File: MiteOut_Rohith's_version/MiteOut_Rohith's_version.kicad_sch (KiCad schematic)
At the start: 28 parts, among them J1 JST, U1 ESP32-S3-WROOM-1, U2 INA260, U3 BQ25185DLHR, U4 TPS61022

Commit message: finished batt board
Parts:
- removed J1: JST, Connector_JST:JST_XH_S2B-XH-A_1x02_P2.50mm_Horizontal, symbol Connector_Generic:Conn_01x02
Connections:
- net IN- is gone; now on net GND: U2.14 (IN-), U2.15 (IN-), U2.16 (IN-)
- net IN+: now also C5.1, U3.2 (BAT)
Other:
- moved on the sheet: C2, C3, C4, D1, D2, D3, D4, D5, R10, R11, R5, R6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

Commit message: quick fix
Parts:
- removed C2: C, symbol Device:C
- removed R5: R, symbol Device:R
- added C6, C7: 22uF, symbol Device:C
- added J1: JST, Connector_JST:JST_XH_S2B-XH-A_1x02_P2.50mm_Horizontal, symbol Connector_Generic:Conn_01x02
- added R13: 732k, symbol Device:R
- added R14: 100k, symbol Device:R
- added R15: 22k, symbol Device:R
- added SW1: SW_SPST, symbol Switch:SW_SPST
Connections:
- net GND: now also C5.1, D3.2 (A), C6.1, C6.2, C7.1, C7.2, J1.2 (Pin_2), R13.1, R14.1, R15.2, SW1.1 (A); no longer C5.2
- net IN+: now also C5.2, J1.1 (Pin_1); no longer C5.1
- net VBUS: now reaches D5.2 (A)
- net V+: now reaches R12.2
- net V+: now also L1.1, U3.1 (SYS), U4.7 (VIN)
- net at D3.1 (K): now also R15.1
- net VIN/Solar+: now reaches D4.2 (A)
- net at U4.3 (VOUT): now also R13.2
- net at U4.4 (FB): now also R14.2
- new net +5V: SW1.2 (B)
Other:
- moved on the sheet: C3, C4, D1, D2, D3, D4, D5, L1, R10, R11, R12, R6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

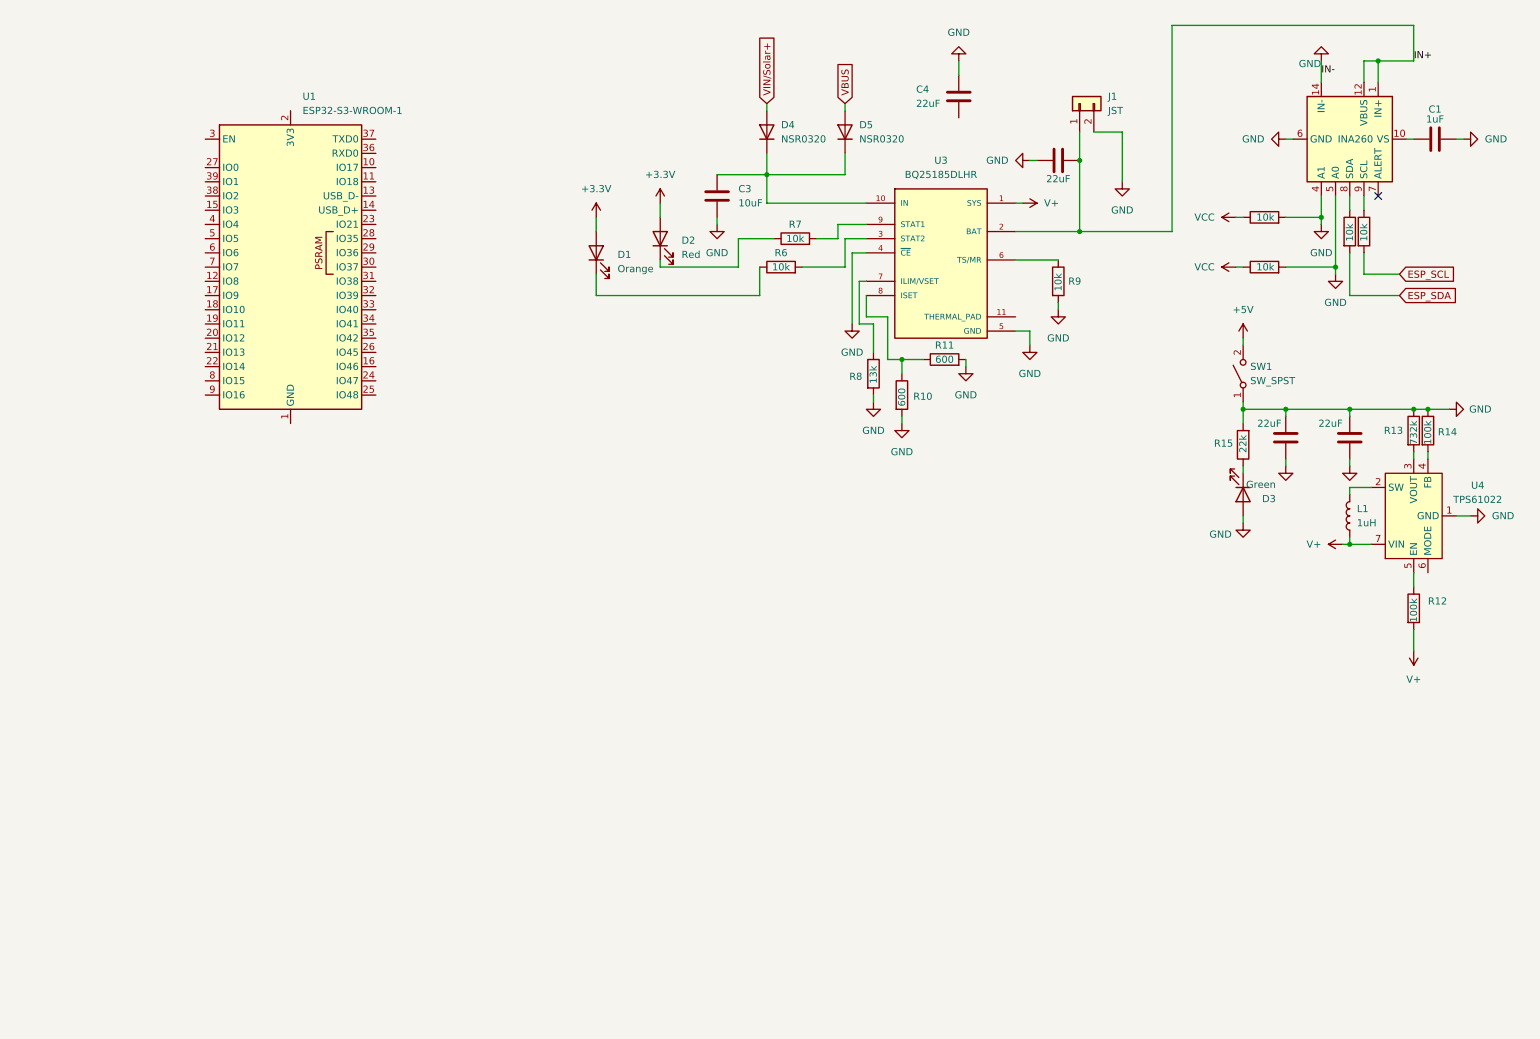
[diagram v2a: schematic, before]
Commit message: added SD Card
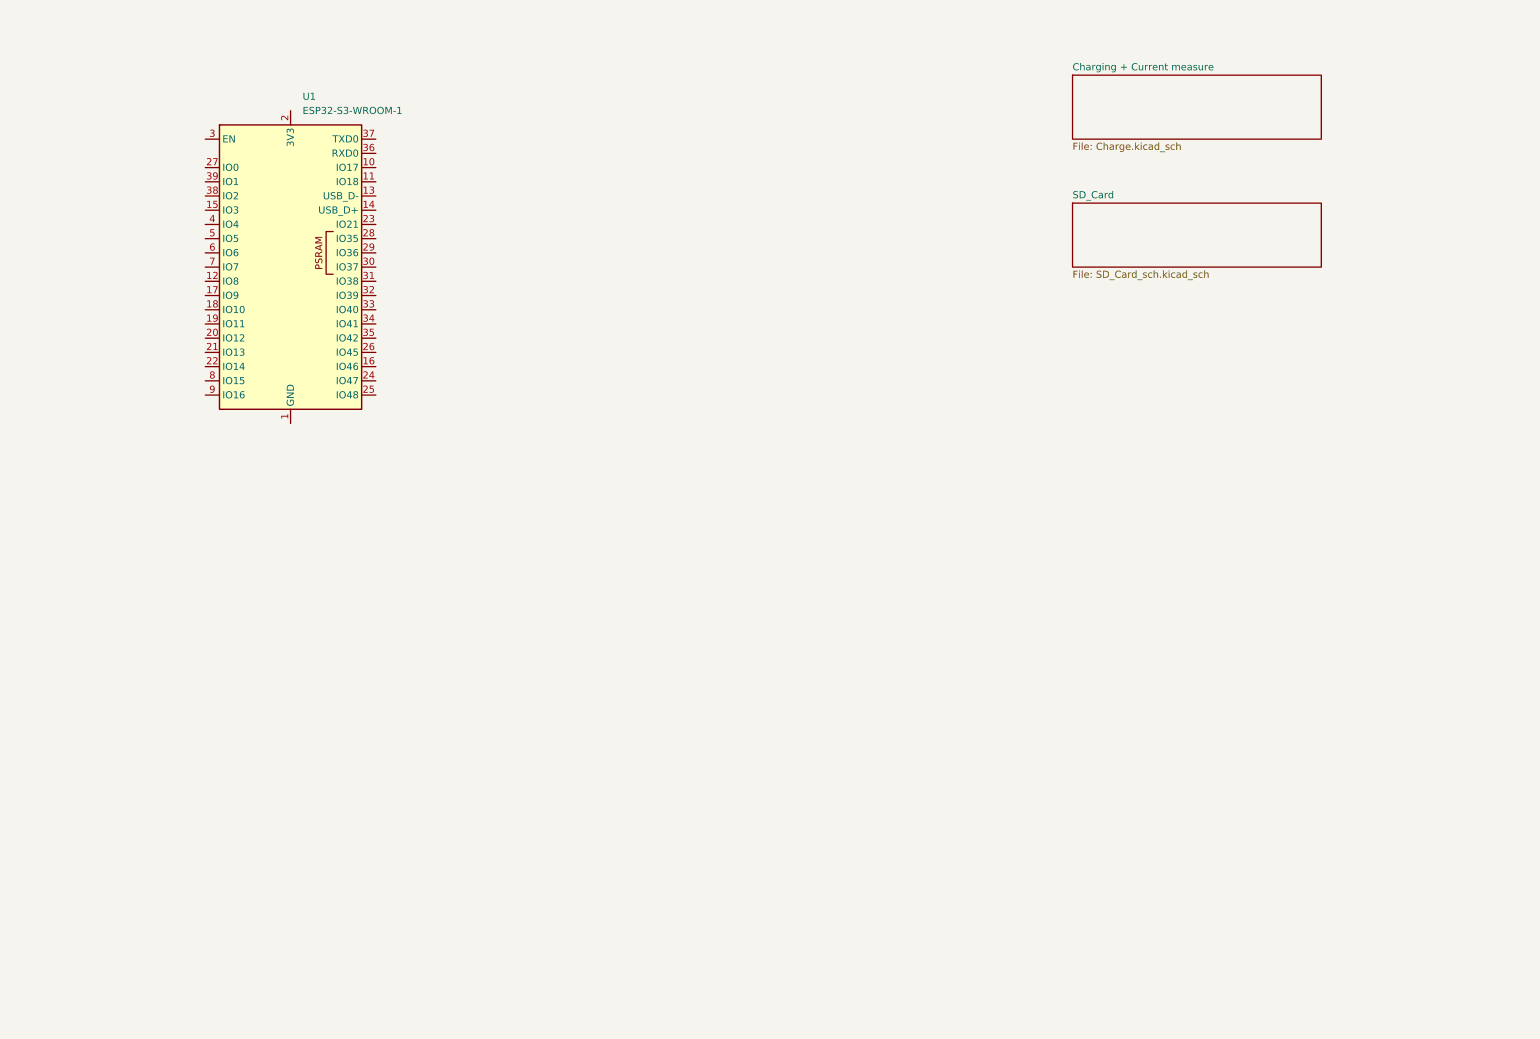
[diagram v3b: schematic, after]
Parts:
- removed C1: 1uF, symbol Device:C
- removed C3: 10uF, symbol Device:C
- removed C4, C5, C6, C7: 22uF, symbol Device:C
- removed D1: Orange, symbol Device:LED
- removed D2: Red, symbol Device:LED
- removed D3: Green, symbol Device:LED
- removed D4, D5: NSR0320, symbol Device:D
- removed J1: JST, Connector_JST:JST_XH_S2B-XH-A_1x02_P2.50mm_Horizontal, symbol Connector_Generic:Conn_01x02
- removed L1: 1uH, symbol Device:L
- removed R1, R2, R3, R4, R6, R7, R9: 10k, symbol Device:R
- removed R10, R11: 600, symbol Device:R
- removed R12, R14: 100k, symbol Device:R
- removed R13: 732k, symbol Device:R
- removed R15: 22k, symbol Device:R
- removed R8: 13k, symbol Device:R
- removed SW1: SW_SPST, symbol Switch:SW_SPST
- removed U2: INA260, Package_SO:TSSOP-16_4.4x5mm_P0.65mm, symbol Sensor_Energy:INA260
- removed U3: BQ25185DLHR, BQ25185DLHR:IC_BQ25185DLHR, symbol BQ25185DLHR:BQ25185DLHR
- removed U4: TPS61022, Package_DFN_QFN:Texas_RWU0007A_VQFN-7_2x2mm_P0.5mm, symbol Converter_DCDC:TPS61022
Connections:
- no-connect marks 1 -> 0
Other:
- added sheet Charging + Current measure (Charge.kicad_sch)
- added sheet SD_Card (SD_Card_sch.kicad_sch)

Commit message: Finished ADC + ESP needing edits
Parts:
- added C18, C19, C21: .1uF, Capacitor_SMD:C_0603_1608Metric_Pad1.08x0.95mm_HandSolder, symbol Device:C
- added C20: 22uf, Capacitor_SMD:C_0603_1608Metric_Pad1.08x0.95mm_HandSolder, symbol Device:C
- added C22, C23: 10uF, symbol Device:C
- added D11: LED, LED_SMD:LED_0603_1608Metric_Pad1.05x0.95mm_HandSolder, symbol Device:LED
- added D4: WS2812B, LED_SMD:LED_WS2812B_PLCC4_5.0x5.0mm_P3.2mm, symbol LED:WS2812B
- added J4: USB_C_Receptacle_USB2.0_16P, Connector_USB:USB_C_Receptacle_GCT_USB4105-xx-A_16P_TopMnt_Horizontal, symbol Connector:USB_C_Receptacle_USB2.0_16P
- added R29, R30, R31: 10k, Resistor_SMD:R_0603_1608Metric_Pad0.98x0.95mm_HandSolder, symbol Device:R
- added R32, R33, R36: 5.1k, symbol Device:R
- added R34: 1M, Resistor_SMD:R_0603_1608Metric_Pad0.98x0.95mm_HandSolder, symbol Device:R
- added R35: 200k, Resistor_SMD:R_0603_1608Metric_Pad0.98x0.95mm_HandSolder, symbol Device:R
- added SW3: RESET, Button_Switch_SMD:SW_SPST_PTS810, symbol Switch:SW_MEC_5E
- added SW4: BOOT, Button_Switch_SMD:SW_SPST_PTS810, symbol Switch:SW_MEC_5E
- added U12: ESP32-S3-MINI-1, RF_Module:ESP32-S2-MINI-1, symbol RF_Module:ESP32-S3-MINI-1
- added U13: D3V3XA4B10LP, Package_DFN_QFN:Diodes_UDFN-10_1x2.5mm_P0.5mm, symbol Power_Protection:D3V3XA4B10LP
- added U14: TLV75801PDRV, Package_SON:WSON-6-1EP_2x2mm_P0.65mm_EP1x1.6mm, symbol Regulator_Linear:TLV75801PDRV
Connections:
- new net: R34.2, R35.1, U14.2 (FB)
- new net: J4.A5 (CC1), R32.1
- new net: J4.B5 (CC2), R33.1
- new net: D4.4 (DIN), U12.30 (IO48)
- new net: D11.1 (K), R36.2
- new net 3V3: C20.1, C21.1, C23.1, D11.2 (A), D4.1 (VDD), R29.1, R30.1, R31.1, R34.1, U12.3 (3V3), U14.1 (OUT)
- new net 5VUSB: C22.1, J4.A4 (VBUS), J4.A9 (VBUS), J4.B4 (VBUS), J4.B9 (VBUS), U13.4, U14.4 (EN), U14.6 (IN)
- new net ESP32_EN: C18.2, R29.2, SW3.3 (K), SW3.4 (A), U12.45 (EN)
- new net GND: C18.1, C19.2, C20.2, C21.2, C22.2, C23.2, D4.3 (VSS), J4.A1 (GND), J4.A12 (GND), J4.B1 (GND), J4.B12 (GND), J4.SH (SHIELD), R32.2, R33.2, R35.2, R36.1, SW3.1, SW3.2, SW4.1, SW4.2, U12.1 (GND), U12.2 (GND), U12.42 (GND), U12.43 (GND), U12.46 (GND), U12.47 (GND), U12.48 (GND), U12.49 (GND), U12.50 (GND), U12.51 (GND), U12.52 (GND), U12.53 (GND), U12.54 (GND), U12.55 (GND), U12.56 (GND), U12.57 (GND), U12.58 (GND), U12.59 (GND), U12.60 (GND), U12.61 (GND), U12.62 (GND), U12.63 (GND), U12.64 (GND), U12.65 (GND), U13.3 (VSS), U13.8 (VSS), U14.3 (GND), U14.7 (GND)
- new net GPIO0: C19.1, SW4.3 (K), SW4.4 (A), U12.4 (IO0)
- new net I2C_SCL: R31.2, U12.21 (IO17)
- new net I2C_SDA: R30.2, U12.22 (IO18)
- new net USB_N: J4.A7 (D-), J4.B7 (D-), U12.23 (USB_D-), U13.2
- new net USB_P: J4.A6 (D+), J4.B6 (D+), U12.24 (USB_D+), U13.1
- no-connect marks 0 -> 2
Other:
- added sheet ADC (ADC.kicad_sch)
- moved on the sheet: U1

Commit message: finished RTC
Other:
- added sheet BME+RTC (BME_RTC.kicad_sch)
- moved on the sheet: C22, C23, D11, J4, R32, R33, R34, R35, R36, U1, U13, U14

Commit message: some changes ig
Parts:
- removed C21: .1uF, Capacitor_SMD:C_0603_1608Metric_Pad1.08x0.95mm_HandSolder, symbol Device:C
- removed D4: WS2812B, LED_SMD:LED_WS2812B_PLCC4_5.0x5.0mm_P3.2mm, symbol LED:WS2812B
- removed R29, R30, R31: 10k, Resistor_SMD:R_0603_1608Metric_Pad0.98x0.95mm_HandSolder, symbol Device:R
- removed SW3: RESET, Button_Switch_SMD:SW_SPST_PTS810, symbol Switch:SW_MEC_5E
- removed SW4: BOOT, Button_Switch_SMD:SW_SPST_PTS810, symbol Switch:SW_MEC_5E
- removed U12: ESP32-S3-MINI-1, RF_Module:ESP32-S2-MINI-1, symbol RF_Module:ESP32-S3-MINI-1
- added C: .1uF, symbol Device:C
- added C16: 22uF, symbol Device:C
- added C17: 10uF, symbol Device:C
- added R14: 10k, symbol Device:R
- added R15: 100, symbol Device:R
- added SW3, SW4: SW_Push, symbol Switch:SW_Push
- added U16: AMS1117CS-3.3, Package_SO:SOIC-8_3.9x4.9mm_P1.27mm, symbol Regulator_Linear:AMS1117CS-3.3
- C18: value .1uF -> 22uF; footprint Capacitor_SMD:C_0603_1608Metric_Pad1.08x0.95mm_HandSolder -> (none)
- C19: footprint Capacitor_SMD:C_0603_1608Metric_Pad1.08x0.95mm_HandSolder -> (none)
- C20: value 22uf -> 1uF; footprint Capacitor_SMD:C_0603_1608Metric_Pad1.08x0.95mm_HandSolder -> (none)
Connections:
- net ESP32_EN is gone; now on net GND: C18.2
- net GPIO0 is gone; now on net +3.3V: C19.1
- net 3V3: no longer C20.1
- net GND: now also U1.1 (GND), U1.40 (GND), U1.41 (GND), C.1, C16.2, C17.1, SW3.1, SW4.1, U16.1 (GND); no longer C18.1
- net +3.3V: now reaches U1.2 (3V3)
- net +3.3V: now also C18.1, C20.1, C.2, C16.1, R14.2, SW3.2, U16.2 (VO), U16.3 (VO), U16.6 (VO), U16.7 (VO)
- net at U1.3 (EN): now also R14.1
- new net: R15.2, SW4.2
- new net +5V: C17.2, U16.4 (VI)
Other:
- moved on the sheet: J4, R32, R33, U1, U13

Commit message: Full Schematic Draft 1
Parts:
- added J9: Conn_01x20_Pin, symbol Connector:Conn_01x20_Pin
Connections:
- net Load_SCL: now reaches U1.10 (IO17)
- net Load_SDA: now reaches U1.11 (IO18)
- net SD_DataOut: now reaches U1.12 (IO8)
- net Data-: now reaches U1.13 (USB_D-)
- net Data+: now reaches U1.14 (USB_D+)
- net GPIO3: now reaches U1.15 (IO3)
- net GPIO3: now also J9.6 (Pin_6)
- net at U1.16 (IO46): now also J9.11 (Pin_11)
- net SD_DataIn: now reaches U1.17 (IO9)
- net SD_CLK: now reaches U1.18 (IO10)
- net CS: now reaches U1.19 (IO11)
- net at U1.20 (IO12): now also J9.1 (Pin_1)
- net at U1.21 (IO13): now also J9.2 (Pin_2)
- net at U1.22 (IO14): now also J9.3 (Pin_3)
- net at U1.23 (IO21): now also J9.18 (Pin_18)
- net at U1.24 (IO47): now also J9.10 (Pin_10)
- net at U1.25 (IO48): now also J9.9 (Pin_9)
- net at U1.26 (IO45): now also J9.12 (Pin_12)
- net at U1.27 (IO0): now also R15.1
- net at U1.31 (IO38): now also J9.17 (Pin_17)
- net at U1.32 (IO39): now also J9.16 (Pin_16)
- net at U1.33 (IO40): now also J9.15 (Pin_15)
- net at U1.34 (IO41): now also J9.14 (Pin_14)
- net at U1.35 (IO42): now also J9.13 (Pin_13)
- net at U1.36 (RXD0): now also J9.19 (Pin_19)
- net at U1.37 (TXD0): now also J9.20 (Pin_20)
- net GPIO2: now reaches U1.38 (IO2)
- net GPIO2: now also J9.7 (Pin_7)
- net GPIO1: now reaches U1.39 (IO1)
- net GPIO1: now also J9.8 (Pin_8)
- net BME(1&2)SDA: now reaches U1.4 (IO4)
- net BME(1&2)SCL: now reaches U1.5 (IO5)
- net BME(3&4)SDA: now reaches U1.6 (IO6)
- net BME(3&4)SCL: now reaches U1.7 (IO7)
- net at U1.8 (IO15): now also J9.4 (Pin_4)
- net at U1.9 (IO16): now also J9.5 (Pin_5)
- no-connect marks 2 -> 5
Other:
- sheet ADC ports: added DataOut, Rate, SCK; removed none
- sheet BME+RTC ports: added BME1SCL, BME1SDA, BME2SCL, BME2SDA, BME3SCL, BME3SDA, BME4SCL, BME4SDA, RTC_SCLK, RTC_SDA, SQW; removed none
- sheet Charging + Current measure ports: added SCK, SDA, VBUS, VIN/Solar+; removed none
- sheet SD_Card ports: added CLK, CS, DataIn, DataOut; removed none
- moved on the sheet: C, C18, C19, C20, C22, C23, D11, R14, R15, R34, R35, R36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

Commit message: some error fixes
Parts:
- renumbered C to C25
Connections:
- net USB_N is gone; now on net Data-: J4.A7 (D-), J4.B7 (D-), U13.2
- net USB_P is gone; now on net Data+: J4.A6 (D+), J4.B6 (D+), U13.1
- net 5VUSB: now also U13.7 (NC)
- net Data+: now also U13.10 (NC)
- net Data-: now also U13.9 (NC)
- no-connect marks 5 -> 7
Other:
- note added: "Notes: - Voltages and Nets for all sheets - SD Card 5V??? - Choose ESP LDO - BME doubled up GPIO - Multi sensor on RTC and single SDA pin"
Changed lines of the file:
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@@
 	(generator_version "10.0")
 	(paper "A4")
+	(text "Notes: \n- Voltages and Nets for all sheets\n- SD Card 5V???\n- Choose ESP LDO\n- BME doubled up GPIO\n- Multi sensor on RTC and single SDA pin"
+		(exclude_from_sim no)
+		(at 164.846 28.702 0)
+		(effects
+			(font
+				(size 2.54 2.54)
+			)
+		)
+	)
 	(junction
 		(at 223.52 74.93)
@@
 	)
 	(junction
-		(at 232.41 99.06)
+		(at 52.07 167.64)
+		(diameter 0)
+		(color 0 0 0 0)
+	)
+	(junction
+		(at 49.53 146.05)
 		(diameter 0)
 		(color 0 0 0 0)
@@
 	)
 	(junction
+		(at 52.07 151.13)
+		(diameter 0)
+		(color 0 0 0 0)
+	)
+	(junction
 		(at 232.41 96.52)
 		(diameter 0)
@@
 	)
 	(junction
+		(at 82.55 172.72)
+		(diameter 0)
+		(color 0 0 0 0)
+	)
+	(junction
 		(at 49.53 24.13)
 		(diameter 0)
@@
 	)
 	(junction
+		(at 54.61 177.8)
+		(diameter 0)
+		(color 0 0 0 0)
+	)
+	(junction
 		(at 54.61 49.53)
 		(diameter 0)
@@
 	)
 	(no_connect
+		(at 82.55 182.88)
+	)
+	(no_connect
 		(at 107.95 67.31)
 	)
@@
 		(at 46.99 160.02)
 	)
+	(no_connect
+		(at 82.55 177.8)
+	)
 	(wire
 		(pts
-			(xy 52.07 172.72) (xy 52.07 151.13)
+			(xy 52.07 172.72) (xy 52.07 167.64)
 		)
 		(stroke
@@
 	(wire
 		(pts
+			(xy 52.07 167.64) (xy 57.15 167.64)
+		)
+		(stroke
+			(width 0)
+			(type default)
+		)
+	)
+	(wire
+		(pts
 			(xy 50.8 63.5) (xy 54.61 63.5)
 		)
@@
 	(wire
 		(pts
+			(xy 52.07 167.64) (xy 52.07 151.13)
+		)
+		(stroke
+			(width 0)
+			(type default)
+		)
+	)
+	(wire
+		(pts
 			(xy 82.55 172.72) (xy 85.09 172.72)
 		)
@@
 	(wire
 		(pts
+			(xy 54.61 182.88) (xy 54.61 177.8)
+		)
+		(stroke
+			(width 0)
+			(type default)
+		)
+	)
+	(wire
+		(pts
 			(xy 130.81 49.53) (xy 130.81 67.31)
 		)
@@
 	(wire
 		(pts
-			(xy 57.15 177.8) (xy 49.53 177.8)
-		)
-		(stroke
-			(width 0)
-			(type default)
-		)
-	)
-	(wire
-		(pts
-			(xy 228.6 99.06) (xy 232.41 99.06)
+			(xy 57.15 177.8) (xy 54.61 177.8)
 		)
 		(stroke
@@
 	(wire
 		(pts
-			(xy 232.41 96.52) (xy 232.41 99.06)
+			(xy 57.15 182.88) (xy 54.61 182.88)
+		)
+		(stroke
+			(width 0)
+			(type default)
+		)
+	)
+	(wire
+		(pts
+			(xy 52.07 151.13) (xy 59.69 151.13)
 		)
 		(stroke
@@
 	(wire
 		(pts
+			(xy 54.61 177.8) (xy 49.53 177.8)
+		)
+		(stroke
+			(width 0)
+			(type default)
+		)
+	)
+	(wire
+		(pts
 			(xy 228.6 91.44) (xy 233.68 91.44)
 		)
@@
 	(wire
 		(pts
+			(xy 49.53 146.05) (xy 59.69 146.05)
+		)
+		(stroke
+			(width 0)
+			(type default)
+		)
+	)
+	(wire
+		(pts
 			(xy 107.95 49.53) (xy 130.81 49.53)
 		)
@@
 	(wire
 		(pts
+			(xy 82.55 167.64) (xy 82.55 172.72)
+		)
+		(stroke
+			(width 0)
+			(type default)
+		)
+	)
+	(wire
+		(pts
 			(xy 226.06 35.56) (xy 234.95 35.56)
 		)
@@
 	(wire
 		(pts
-			(xy 232.41 99.06) (xy 232.41 100.33)
+			(xy 232.41 96.52) (xy 232.41 100.33)
 		)
 		(stroke
@@
 		)
 	)
-	(label "USB_N"
-		(at 46.99 146.05 0)
-		(effects
-			(font
-				(size 1.27 1.27)
-			)
-			(justify left bottom)
-		)
-	)
 	(label "3V3"
 		(at 137.16 128.27 0)
@@
 		)
 	)
-	(label "USB_P"
-		(at 46.99 151.13 0)
-		(effects
-			(font
-				(size 1.27 1.27)
-			)
-			(justify left bottom)
-		)
-	)
 	(label "5VUSB"
 		(at 96.52 128.27 0)
@@
 		)
 	)
+	(global_label "Data+"
+		(shape input)
+		(at 59.69 151.13 0)
+		(fields_autoplaced yes)
+		(effects
+			(font
+				(size 1.27 1.27)
+			)
+			(justify left)
+		)
+		(property "Intersheetrefs" "${INTERSHEET_REFS}"
+			(at 68.5413 151.13 0)
+			(hide yes)
+			(show_name no)
+			(do_not_autoplace no)
+			(effects
+				(font
+					(size 1.27 1.27)
+				)
+				(justify left)
+			)
+		)
+	)
+	(global_label "Data-"
+		(shape input)
+		(at 59.69 146.05 0)
+		(fields_autoplaced yes)
+		(effects
+			(font
+				(size 1.27 1.27)
+			)
+			(justify left)
+		)
+		(property "Intersheetrefs" "${INTERSHEET_REFS}"
+			(at 68.5413 146.05 0)
+			(hide yes)
+			(show_name no)
+			(do_not_autoplace no)
+			(effects
+				(font
+					(size 1.27 1.27)
+				)
+				(justify left)
+			)
+		)
+	)
 	(global_label "SD_CLK"
 		(shape input)
@@
 		(in_pos_files yes)
 		(dnp no)
-		(property "Reference" "C"
+		(property "Reference" "C25"
 			(at 43.434 66.04 90)
+			(hide yes)
 			(show_name no)
 			(do_not_autoplace no)
@@
 			(project "MiteOut_Rohith's_version"
 				(path "/02ec46d8-9fff-42fd-88ff-c4cb11c6dc1b"
-					(reference "C")
+					(reference "C25")
 					(unit 1)
 				)
